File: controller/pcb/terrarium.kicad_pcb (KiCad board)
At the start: 2 copper layers, 90 x 90 mm, 37 parts

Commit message: add v1.1 pcb
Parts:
- added R5: R_Small, Resistor_THT:R_Axial_DIN0207_L6.3mm_D2.5mm_P7.62mm_Horizontal, F.Cu at (70.2, 43.7)
- added TP1: TestPoint, TestPoint:TestPoint_Pad_1.5x1.5mm, F.Cu at (66.0, 40.5)
- added TP2: TestPoint, TestPoint:TestPoint_Pad_1.5x1.5mm, F.Cu at (63.4, 40.5)
- R1, R2, R3, R4: footprint Resistor_THT:R_Axial_DIN0204_L3.6mm_D1.6mm_P2.54mm_Vertical -> Resistor_THT:R_Axial_DIN0207_L6.3mm_D2.5mm_P7.62mm_Horizontal
- moved R1 2.93 mm to (110.4, 72.9)
- moved R3 2.16 mm to (83.7, 72.6)
- moved LED1 1.61 mm to (107.7, 72.9)
- moved TR1 0.46 mm to (121.0, 72.9)
- moved R4 0.40 mm to (96.9, 76.6)
- moved R2 0.38 mm to (123.6, 76.7)
- moved TR2 0.38 mm to (94.4, 72.6)
- moved D1 0.25 mm to (123.6, 80.1)
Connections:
- AD1 pad 4: G23 -> Net-(AD1-Pad4)
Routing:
- net Net-(AD1-Pad4): track 0.00 -> 16.1 mm, vias 0 -> 2
- net G23: track 31.1 -> 17.6 mm, vias 2 -> 0
- net Net-(D2-Pad2): track 22.9 -> 19.9 mm
- net Net-(D1-Pad2): track 23.1 -> 20.2 mm
- net Net-(R3-Pad2): track 5.59 -> 3.05 mm
- net Net-(LED2-Pad1): track 4.83 -> 2.67 mm
- net G4: track 41.8 -> 43.8 mm
- net +5V: track 294.8 -> 292.9 mm
- net Net-(R1-Pad2): track 4.95 -> 3.18 mm
- net Net-(LED1-Pad1): track 4.32 -> 2.67 mm

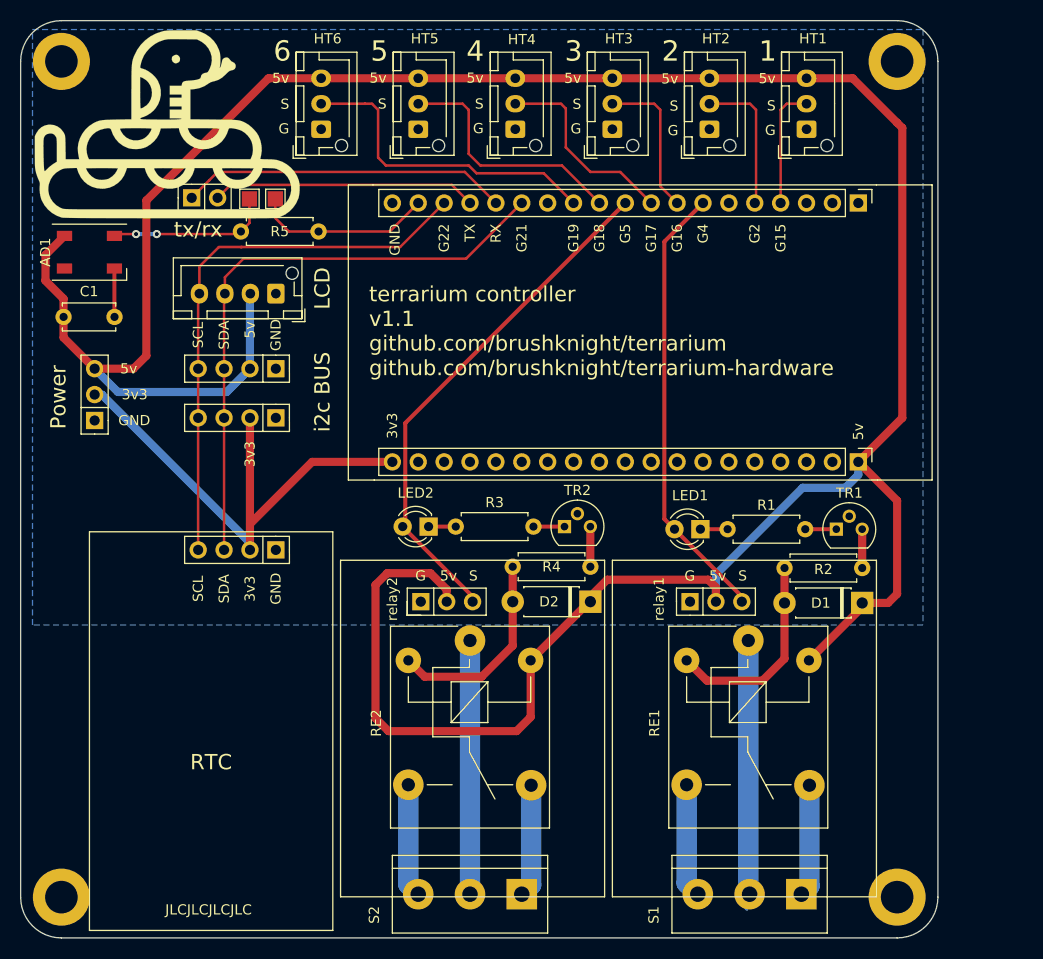
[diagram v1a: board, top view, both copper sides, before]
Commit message: add 3rd relay for lamp
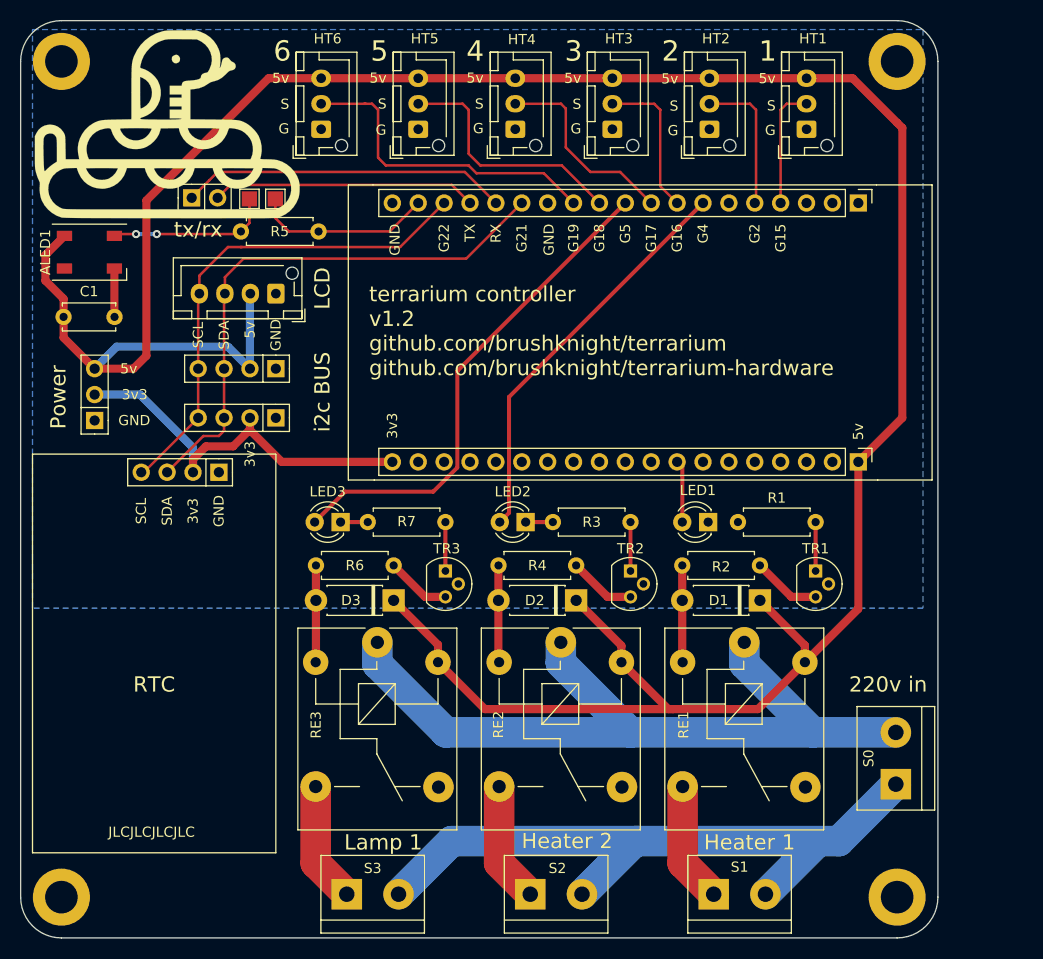
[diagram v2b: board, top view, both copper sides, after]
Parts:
- removed relay1: 1, Connector_PinHeader_2.54mm:PinHeader_1x03_P2.54mm_Vertical
- removed relay2: 2, Connector_PinHeader_2.54mm:PinHeader_1x03_P2.54mm_Vertical
- added D3: 1N47xxA, Diode_THT:D_DO-41_SOD81_P7.62mm_Horizontal, F.Cu at (77.6, 79.9)
- added LED3: ACTIVE, LED_THT:LED_D3.0mm_Clear, F.Cu at (72.4, 72.2)
- added R6: R_Small, Resistor_THT:R_Axial_DIN0207_L6.3mm_D2.5mm_P7.62mm_Horizontal, F.Cu at (77.6, 76.5)
- added R7: R_Small, Resistor_THT:R_Axial_DIN0207_L6.3mm_D2.5mm_P7.62mm_Horizontal, F.Cu at (75.1, 72.2)
- added RE3: SANYOU_SRD_Form_C, Relay_THT:Relay_SPDT_SANYOU_SRD_Series_Form_C, F.Cu at (76.0, 84.0)
- added S0: Power 220 in, TerminalBlock:TerminalBlock_bornier-2_P5.08mm, F.Cu at (126.9, 97.9)
- added S3: Lamp 1 Out, TerminalBlock:TerminalBlock_bornier-2_P5.08mm, F.Cu at (73.0, 108.7)
- added TR3: MMBT3904, Package_TO_SOT_THT:TO-92, F.Cu at (82.7, 77.0)
- S1: value Screw_Terminal_01x03 -> Heater 1 Out; footprint TerminalBlock:TerminalBlock_bornier-3_P5.08mm -> TerminalBlock:TerminalBlock_bornier-2_P5.08mm
- S2: value Screw_Terminal_01x03 -> Heater 2 Out; footprint TerminalBlock:TerminalBlock_bornier-3_P5.08mm -> TerminalBlock:TerminalBlock_bornier-2_P5.08mm
- moved D1 10.0 mm to (113.5, 79.9)
- moved R2 10.0 mm to (113.5, 76.5)
- moved LED2 9.54 mm to (90.6, 72.2)
- moved R3 9.54 mm to (93.2, 72.2)
- moved i2c1 9.45 mm to (60.5, 67.3)
- moved RE2 8.91 mm to (94.0, 84.0)
- moved S1 8.60 mm to (109.0, 108.7), turned to 0 degrees
- moved TR2 7.81 mm to (100.8, 77.0), turned to 270 degrees
- moved TR1 4.58 mm to (119.0, 77.0), turned to 270 degrees
- moved D2 1.40 mm to (95.5, 79.9)
- moved R4 1.40 mm to (95.5, 76.5)
- moved R1 1.23 mm to (111.4, 72.2)
- moved LED1 1.03 mm to (108.5, 72.2)
- moved S2 0.83 mm to (91.0, 108.7), turned to 0 degrees
- moved RE1 0.43 mm to (112.0, 84.0)
- renumbered AD1 to ALED1
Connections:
- LED1 pad 2: G4 -> G14
- LED2 pad 2: G5 -> G4
- RE1 pad 1: Net-(RE1-Pad1) -> 220L
- RE2 pad 1: Net-(RE2-Pad1) -> 220L
- S1 pad 1: Net-(RE1-Pad4) -> Net-(RE1-Pad3)
- S1 pad 2: Net-(RE1-Pad1) -> 220N
- S2 pad 1: Net-(RE2-Pad4) -> Net-(RE2-Pad3)
- S2 pad 2: Net-(RE2-Pad1) -> 220N
- esp32-right1 pad 8: Net-(esp32-right1-Pad8) -> G14
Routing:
- net 220L: track 0.00 -> 79.1 mm
- net 220N: track 0.00 -> 68.2 mm
- net Net-(RE1-Pad1): track 25.7 -> 0.00 mm
- net Net-(RE2-Pad1): track 24.9 -> 0.00 mm
- net +5V: track 292.9 -> 269.3 mm
- net +3V3: track 54.0 -> 38.7 mm
- net Net-(RE3-Pad3): track 0.00 -> 11.8 mm
- net Net-(RE2-Pad4): track 11.1 -> 0.00 mm
- net Net-(RE1-Pad4): track 11.0 -> 0.00 mm
- net Net-(D1-Pad2): track 20.2 -> 9.51 mm
- net Net-(D2-Pad2): track 19.9 -> 9.52 mm
- net Net-(D3-Pad2): track 0.00 -> 9.51 mm
- net Net-(R6-Pad1): track 0.00 -> 6.36 mm
- net G14: track 0.00 -> 6.12 mm
- net SCL: track 54.8 -> 49.1 mm
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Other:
- board text added: "220v in"
- board text added: "Heater 1"
- board text added: "Heater 2"
- board text added: "Lamp 1"
- board text added: "terrarium controller v1.2 github.com/brushknight/terrarium github.com/brushknight/terrarium-hardware"
- board text removed: "terrarium controller v1.1 github.com/brushknight/terrarium github.com/brushknight/terrarium-hardware"

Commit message: final changes in pcb v1.2
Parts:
- removed TP1, TP2: TestPoint, TestPoint:TestPoint_Pad_1.5x1.5mm
- removed rxtx1: Conn_01x02, Connector_PinSocket_2.54mm:PinSocket_1x02_P2.54mm_Vertical
- TR1, TR2, TR3: footprint Package_TO_SOT_THT:TO-92 -> Package_TO_SOT_THT:TO-92_Inline
- moved i2c2 7.62 mm to (58.4, 49.8), turned to 0 degrees
- moved R5 5.22 mm to (75.4, 43.3)
- moved HT1 4.99 mm to (118.1, 28.7), turned to 270 degrees
- moved HT2 4.99 mm to (108.6, 28.7), turned to 270 degrees
- moved HT3 4.99 mm to (99.1, 28.7), turned to 270 degrees
- moved HT4 4.99 mm to (89.5, 28.7), turned to 270 degrees
- moved HT5 4.99 mm to (80.0, 28.7), turned to 270 degrees
- moved HT6 4.99 mm to (70.5, 28.7), turned to 270 degrees
- moved esp32-left1 2.50 mm to (125.7, 40.9)
- moved esp32-right1 2.50 mm to (125.7, 66.3)
- moved TR1 0.55 mm to (119.0, 76.5)
- moved TR2 0.55 mm to (100.8, 76.5)
- moved TR3 0.55 mm to (82.7, 76.5)
- moved S1 0.50 mm to (109.5, 108.7)
- moved S2 0.50 mm to (91.5, 108.7)
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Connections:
- HT1 pad 1: GND -> +5V
- HT1 pad 3: +5V -> GND
- HT2 pad 1: GND -> +5V
- HT2 pad 3: +5V -> GND
- HT3 pad 1: GND -> +5V
- HT3 pad 3: +5V -> GND
- HT4 pad 1: GND -> +5V
- HT4 pad 3: +5V -> GND
- HT5 pad 1: GND -> +5V
- HT5 pad 3: +5V -> GND
- HT6 pad 1: GND -> +5V
- HT6 pad 3: +5V -> GND
- TR1 pad 1: Net-(R1-Pad2) -> GND
- TR1 pad 2: GND -> Net-(R1-Pad2)
- TR2 pad 1: Net-(R3-Pad2) -> GND
- TR2 pad 2: GND -> Net-(R3-Pad2)
- TR3 pad 1: Net-(R7-Pad2) -> GND
- TR3 pad 2: GND -> Net-(R7-Pad2)
- i2c2 pad 1: GND -> SCL
- i2c2 pad 2: +5V -> SDA
- i2c2 pad 3: SDA -> +5V
- i2c2 pad 4: SCL -> GND
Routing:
- net RX: track 32.2 -> 0.00 mm
- net TX: track 26.0 -> 0.00 mm
- net G23: track 17.6 -> 8.07 mm
- net Net-(R1-Pad2): track 4.74 -> 9.63 mm
- net Net-(R3-Pad2): track 4.80 -> 9.30 mm
- net Net-(R7-Pad2): track 4.80 -> 9.30 mm
- net Net-(LED1-Pad1): track 0.00 -> 2.92 mm
- net SCL: track 49.1 -> 51.6 mm
- net SDA: track 55.3 -> 57.8 mm
- net G19: track 31.6 -> 34.1 mm
- net G18: track 24.3 -> 26.8 mm
- net +3V3: track 38.7 -> 41.2 mm
- net 220N: track 68.2 -> 70.6 mm
- net Net-(ALED1-Pad4): track 16.1 -> 18.0 mm
- net G5: track 49.0 -> 50.4 mm
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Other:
- board text added: "G14"
- board text added: "G23"
- board text removed: "tx/rx"

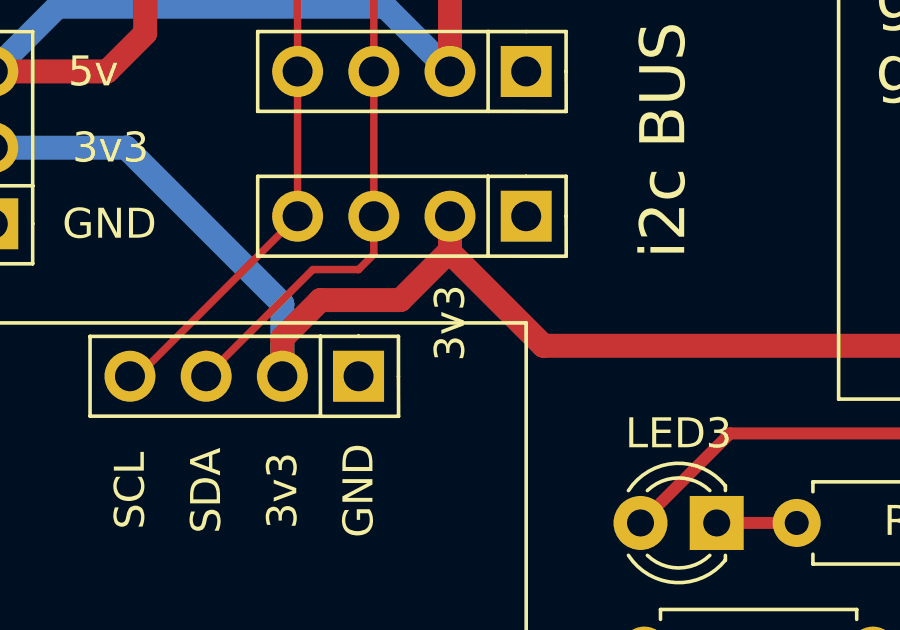
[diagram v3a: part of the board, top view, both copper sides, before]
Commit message: fix labels
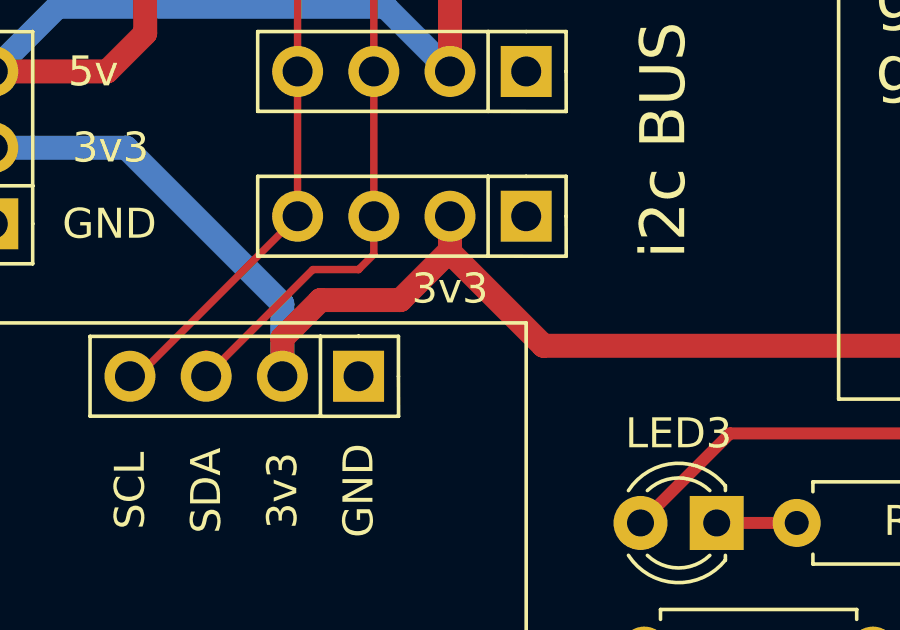
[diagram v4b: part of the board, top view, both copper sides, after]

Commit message: update traces
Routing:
- net G17: track 19.9 -> 21.5 mm

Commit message: pcb v1.2 released
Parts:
- removed TR3: MMBT3904, Package_TO_SOT_THT:TO-92_Inline
- added Q3: S8050, Package_TO_SOT_THT:TO-92_Inline, F.Cu at (82.7, 76.5)
- Q1: renamed from TR1; value MMBT3904 -> S8050
- Q2: renamed from TR2; value MMBT3904 -> S8050
- R1, R3, R5, R7: value R_Small -> 150ohm
- S1: value Heater 1 Out -> Lamp 1 Out
- S2: value Heater 2 Out -> Heater 1 Out
- S3: value Lamp 1 Out -> Heater 2 Out
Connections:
- HT1 pad 2: G15 -> G27
- HT2 pad 2: G2 -> G26
- LED1 pad 2: G14 -> G25
- esp32-left1 pad 4: G15 -> Net-(esp32-left1-Pad4)
- esp32-left1 pad 5: G2 -> Net-(esp32-left1-Pad5)
- esp32-right1 pad 10: Net-(esp32-right1-Pad10) -> G26
- esp32-right1 pad 11: Net-(esp32-right1-Pad11) -> G25
- esp32-right1 pad 8: G14 -> Net-(esp32-right1-Pad8)
- esp32-right1 pad 9: Net-(esp32-right1-Pad9) -> G27
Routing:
- net G27: track 0.00 -> 42.0 mm
- net G26: track 0.00 -> 41.3 mm
- net G2: track 14.9 -> 0.00 mm
- net G15: track 13.0 -> 0.00 mm
- net G25: track 0.00 -> 9.39 mm
- net G14: track 6.73 -> 0.00 mm
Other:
- board text added: "G25"
- board text added: "G26"
- board text added: "G27"
- board text removed: "G14"
- board text removed: "G15"
- board text removed: "G2"

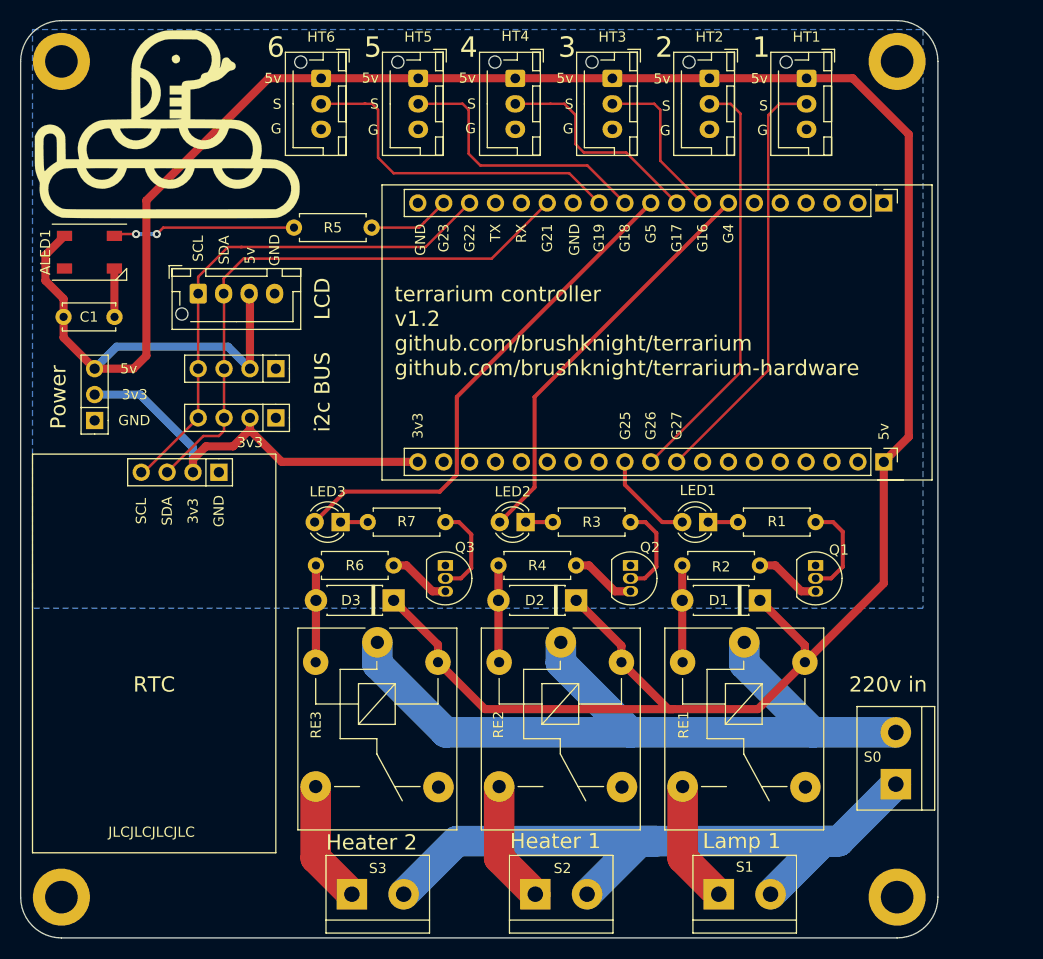
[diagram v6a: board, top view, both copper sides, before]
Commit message: pcb: add rtc ds3231m
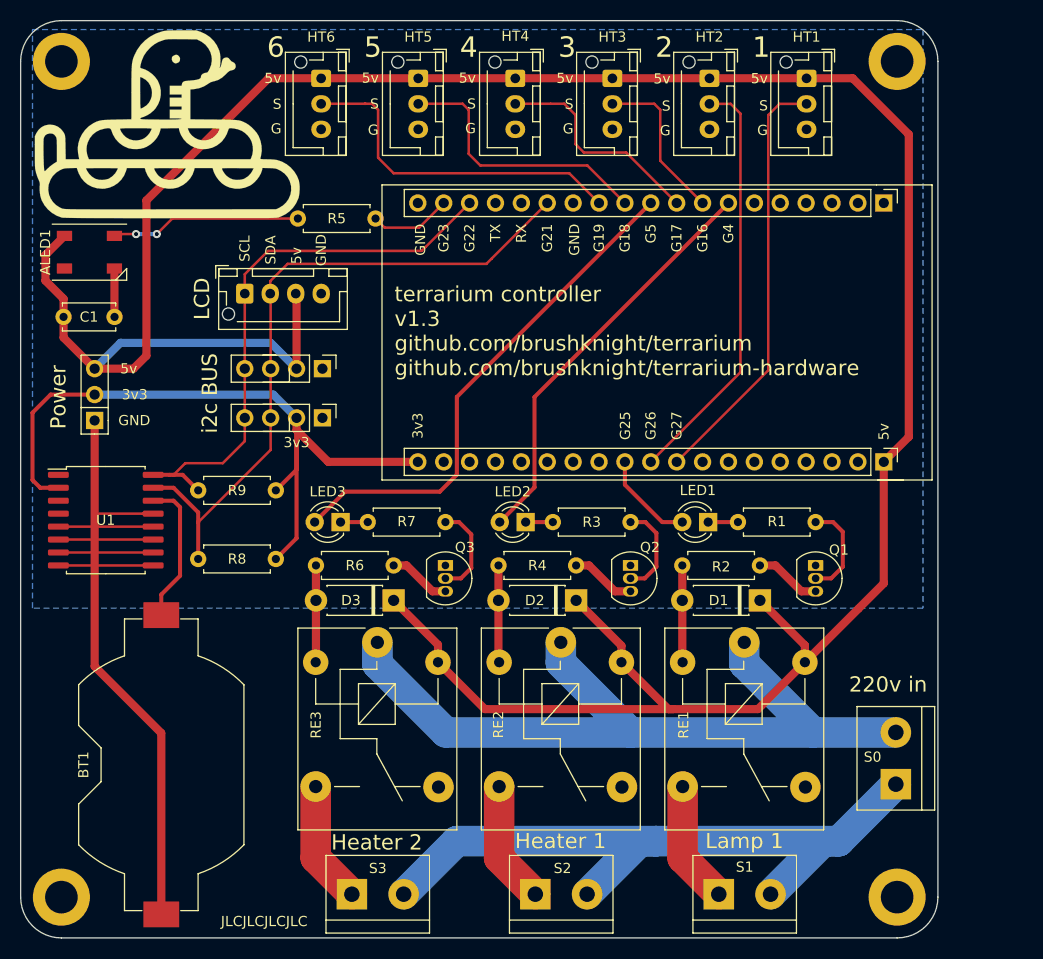
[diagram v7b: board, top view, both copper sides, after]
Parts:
- removed i2c1: RTC, Connector_PinHeader_2.54mm:PinHeader_1x04_P2.54mm_Vertical
- added BT1: LIR2032, Battery:BatteryHolder_Keystone_1058_1x2032, F.Cu at (54.8, 96.0)
- added R8: 4.7k, Resistor_THT:R_Axial_DIN0207_L6.3mm_D2.5mm_P7.62mm_Horizontal, F.Cu at (66.0, 75.8)
- added R9: 4.7k, Resistor_THT:R_Axial_DIN0207_L6.3mm_D2.5mm_P7.62mm_Horizontal, F.Cu at (58.4, 69.1)
- added U1: DS3231M, Package_SO:SOIC-16W_7.5x10.3mm_P1.27mm, F.Cu at (49.4, 72.0)
- moved i2c2 4.57 mm to (63.0, 49.8)
- moved i2c3 4.57 mm to (70.6, 57.1)
- moved i2c4 4.57 mm to (70.6, 62.0)
- moved R5 0.97 mm to (75.8, 42.4)
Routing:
- net GND: track 4.75 -> 117.5 mm
- net +3V3: track 41.2 -> 74.1 mm
- net Net-(BT1-Pad1): track 0.00 -> 14.3 mm
- net SDA: track 57.8 -> 67.2 mm
- net +5V: track 269.8 -> 274.7 mm
- net SCL: track 51.6 -> 55.0 mm
- net Net-(ALED1-Pad4): track 18.0 -> 18.7 mm
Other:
- board text added: "terrarium controller v1.3 github.com/brushknight/terrarium github.com/brushknight/terrarium-hardware"
- board text removed: "RTC"
- board text removed: "terrarium controller v1.2 github.com/brushknight/terrarium github.com/brushknight/terrarium-hardware"
